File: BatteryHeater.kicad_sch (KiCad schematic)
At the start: 15 parts, among them Q5 Si1442DH, Q7 Si1442DH, Q9 Si1442DH

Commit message: More updates
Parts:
- removed Q5, Q7, Q9: Si1442DH, Package_TO_SOT_SMD:SOT-363_SC-70-6, symbol Transistor_FET:Si1442DH
- removed R23, R27, R31: 10k, Resistor_SMD:R_0603_1608Metric, symbol Device:R_Small
- added D10: GREEN, LED_SMD:LED_0603_1608Metric, symbol Device:LED_Small
- added Q10: IRLML2803, Package_TO_SOT_SMD:SOT-23, symbol Argus-IC:IRLML2803
- added Q19: SIRA99DP-T1-GE3, Package_SO:PowerPAK_SO-8_Single, symbol Transistor_FET:Si7141DP
- added R14, R16: 10k, Resistor_SMD:R_0603_1608Metric, symbol Device:R_Small
- added R15: 1k, Resistor_SMD:R_0603_1608Metric, symbol Device:R_Small
- added R17: 2.7k, Resistor_SMD:R_0603_1608Metric, symbol Device:R_Small
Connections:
- net ENABLE: now also R14.2, R15.2
- net SYSTEM_VSS: now also R22.1, R26.1, R30.1
- net VBUS: now also Q19.1 (S), Q19.2 (S), Q19.3 (S), R16.2; no longer R20.2, R24.2, R28.2
- new net: D10.2 (A), R17.1
- new net: Q10.1 (G), R15.1
- new net: Q10.3 (D), Q19.4 (G), R16.1
- new net GND: D10.1 (K), Q10.2 (S), R14.1
- new net V_HEATER: Q19.5 (D), R17.2, R20.2, R24.2, R28.2
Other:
- moved on the sheet: R20, R21, R22, R24, R25, R26, R28, R29, R30

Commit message: Finalized updates with recommendations and exported files
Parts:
- added F11: 2A, Fuse:Fuse_1206_3216Metric, symbol Device:Fuse_Small
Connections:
- net VBUS: now also F11.1; no longer Q19.1 (S), Q19.2 (S), Q19.3 (S), R16.2
- new net: F11.2, Q19.1 (S), Q19.2 (S), Q19.3 (S), R16.2
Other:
- moved on the sheet: R16

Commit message: uncommitted changes
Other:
- note added: "#TODO Update to larger resistor footprint"
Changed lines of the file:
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@@
+		)
+	)
+	(text "#TODO Update to larger resistor footprint"
+		(exclude_from_sim no)
+		(at 236.22 103.124 0)
+		(effects
+			(font
+				(size 1.27 1.27)
+			)
 		)
 	)
 	(label "V_HEATER"
 		(at 147.32 83.82 0)
+		(fields_autoplaced yes)
 		(effects
 			(font
@@
 		(shape input)
 		(at 80.01 101.6 180)
+		(fields_autoplaced yes)
 		(effects
 			(font

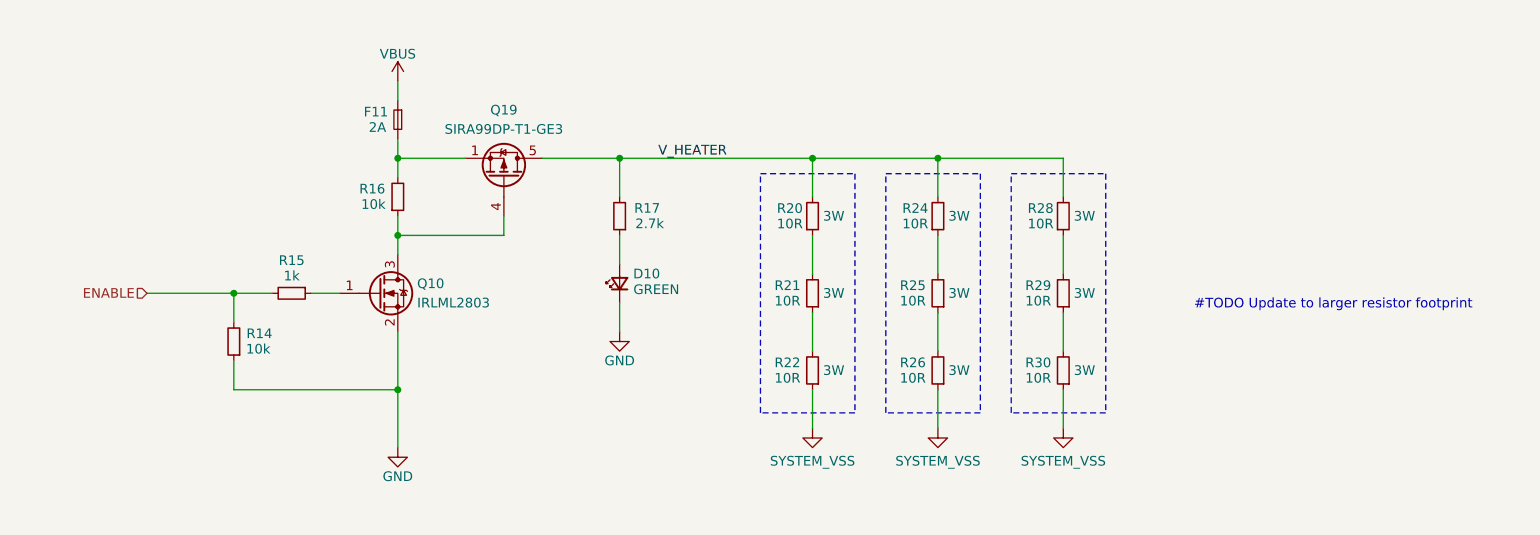
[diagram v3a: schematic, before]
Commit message: Updated FPC connector
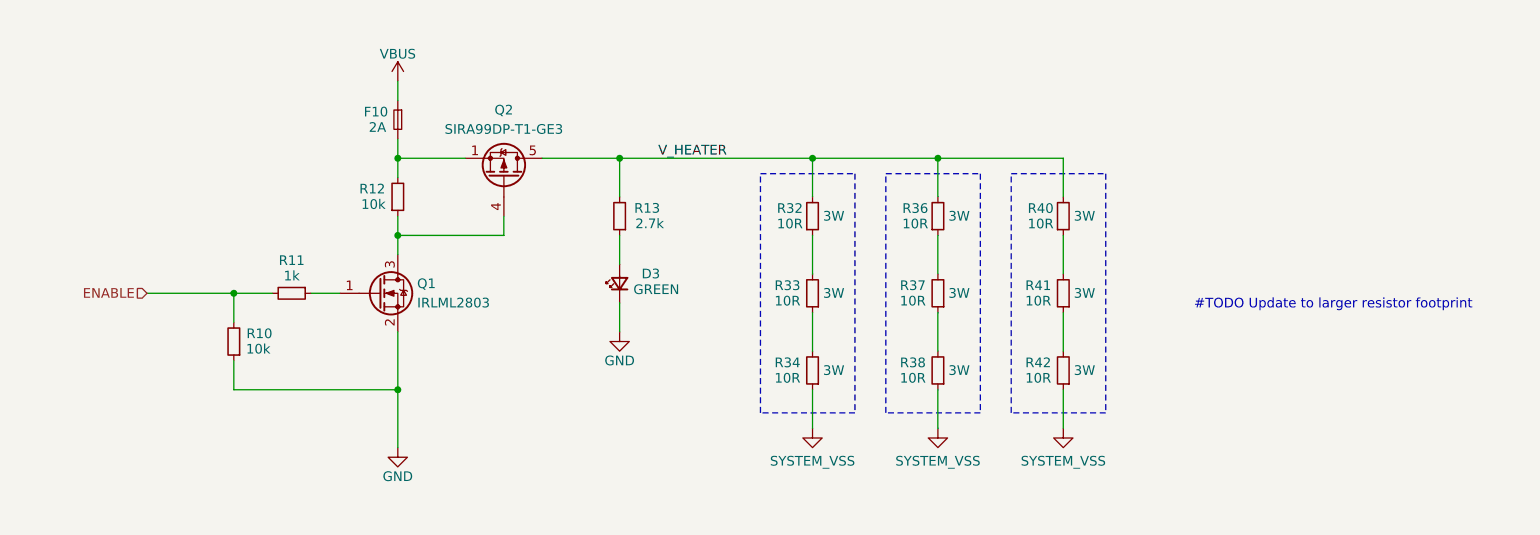
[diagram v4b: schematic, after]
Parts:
- renumbered D10 to D3, F11 to F10, Q10 to Q1, Q19 to Q2, R14 to R10, R15 to R11, R16 to R12, R17 to R13, R20 to R32, R21 to R33, R22 to R34, R24 to R36, R25 to R37, R26 to R38, R28 to R40, R29 to R41, R30 to R42
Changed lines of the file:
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@@
 (kicad_sch
-	(version 20231120)
+	(version 20250114)
 	(generator "eeschema")
-	(generator_version "8.0")
+	(generator_version "9.0")
 	(paper "A4")
 	(title_block
@@
 		(comment 3 "V. Rajesh")
 	)
+	(rectangle
+		(start 177.292 85.852)
+		(end 189.738 117.348)
+		(stroke
+			(width 0)
+			(type dash)
+		)
+		(fill
+			(type none)
+		)
+	)
+	(rectangle
+		(start 193.802 85.852)
+		(end 206.248 117.348)
+		(stroke
+			(width 0)
+			(type dash)
+		)
+		(fill
+			(type none)
+		)
+	)
+	(rectangle
+		(start 160.782 85.852)
+		(end 173.228 117.348)
+		(stroke
+			(width 0)
+			(type dash)
+		)
+		(fill
+			(type none)
+		)
+	)
+	(text "#TODO Update to larger resistor footprint"
+		(exclude_from_sim no)
+		(at 236.22 103.124 0)
+		(effects
+			(font
+				(size 1.27 1.27)
+			)
+		)
+	)
 	(junction
 		(at 113.03 83.82)
@@
 		)
 	)
-	(rectangle
-		(start 177.292 85.852)
-		(end 189.738 117.348)
-		(stroke
-			(width 0)
-			(type dash)
-		)
-		(fill
-			(type none)
-		)
-	)
-	(rectangle
-		(start 193.802 85.852)
-		(end 206.248 117.348)
-		(stroke
-			(width 0)
-			(type dash)
-		)
-		(fill
-			(type none)
-		)
-	)
-	(rectangle
-		(start 160.782 85.852)
-		(end 173.228 117.348)
-		(stroke
-			(width 0)
-			(type dash)
-		)
-		(fill
-			(type none)
-		)
-	)
-	(text "#TODO Update to larger resistor footprint"
-		(exclude_from_sim no)
-		(at 236.22 103.124 0)
+	(label "V_HEATER"
+		(at 147.32 83.82 0)
 		(effects
 			(font
 				(size 1.27 1.27)
 			)
-		)
-	)
-	(label "V_HEATER"
-		(at 147.32 83.82 0)
-		(fields_autoplaced yes)
-		(effects
-			(font
-				(size 1.27 1.27)
-			)
 			(justify left bottom)
 		)
@@
 		(shape input)
 		(at 80.01 101.6 180)
-		(fields_autoplaced yes)
 		(effects
 			(font
@@
 		(on_board yes)
 		(dnp no)
-		(property "Reference" "R28"
+		(property "Reference" "R40"
 			(at 199.39 90.424 0)
 			(effects
@@
 		(on_board yes)
 		(dnp no)
-		(property "Reference" "R17"
+		(property "Reference" "R13"
 			(at 147.574 89.662 0)
 			(effects
@@
 		(on_board yes)
 		(dnp no)
-		(property "Reference" "#PWR014"
+		(property "Reference" "#PWR057"
 			(at 167.64 125.73 0)
 			(effects
@@
 		(on_board yes)
 		(dnp no)
-		(property "Reference" "Q10"
+		(property "Reference" "Q1"
 			(at 115.57 100.33 0)
 			(effects
@@
 		(on_board yes)
 		(dnp no)
-		(property "Reference" "R14"
+		(property "Reference" "R10"
 			(at 96.52 106.172 0)
 			(effects
@@
 		(on_board yes)
 		(dnp no)
-		(property "Reference" "R25"
+		(property "Reference" "R37"
 			(at 180.848 100.584 0)
 			(effects
@@
 		(on_board yes)
 		(dnp no)
-		(property "Reference" "R15"
+		(property "Reference" "R11"
 			(at 99.06 97.282 90)
 			(effects
@@
 		(on_board yes)
 		(dnp no)
-		(property "Reference" "R29"
+		(property "Reference" "R41"
 			(at 197.358 100.584 0)
 			(effects
@@
 		(on_board yes)
 		(dnp no)
-		(property "Reference" "R22"
+		(property "Reference" "R34"
 			(at 164.338 110.744 0)
 			(effects
@@
 		(on_board yes)
 		(dnp no)
-		(property "Reference" "R26"
+		(property "Reference" "R38"
 			(at 180.848 110.744 0)
 			(effects
@@
 		(on_board yes)
 		(dnp no)
-		(property "Reference" "#PWR024"
+		(property "Reference" "#PWR023"
 			(at 200.66 125.73 0)
 			(effects
@@
 		(on_board yes)
 		(dnp no)
-		(property "Reference" "F11"
+		(property "Reference" "F10"
 			(at 111.76 77.724 90)
 			(effects
@@
 		(on_board yes)
 		(dnp no)
-		(property "Reference" "#PWR015"
+		(property "Reference" "#PWR09"
 			(at 113.03 77.47 0)
 			(effects
@@
 		(on_board yes)
 		(dnp no)
-		(property "Reference" "R24"
+		(property "Reference" "R36"
 			(at 182.88 90.424 0)
 			(effects
@@
 		(on_board yes)
 		(dnp no)
-		(property "Reference" "R20"
+		(property "Reference" "R32"
 			(at 166.37 90.424 0)
 			(effects
@@
 		(on_board yes)
 		(dnp no)
-		(property "Reference" "Q19"
+		(property "Reference" "Q2"
 			(at 127 77.47 90)
 			(effects
@@
 		(on_board yes)
 		(dnp no)
-		(property "Reference" "R30"
+		(property "Reference" "R42"
 			(at 197.358 110.744 0)
 			(effects
@@
 		(on_board yes)
 		(dnp no)
-		(property "Reference" "#GND04"
+		(property "Reference" "#GND01"
 			(at 113.03 121.92 0)
 			(effects
@@
 		(on_board yes)
 		(dnp no)
-		(property "Reference" "D10"
+		(property "Reference" "D3"
 			(at 147.574 98.298 90)
 			(effects
@@
 		(on_board yes)
 		(dnp no)
-		(property "Reference" "R16"
+		(property "Reference" "R12"
 			(at 107.95 87.122 0)
 			(effects
@@
 		(on_board yes)
 		(dnp no)
-		(property "Reference" "#GND05"
+		(property "Reference" "#GND03"
 			(at 142.24 106.68 0)
 			(effects
@@
 		(on_board yes)
 		(dnp no)
-		(property "Reference" "#PWR018"
+		(property "Reference" "#PWR017"
 			(at 184.15 125.73 0)
 			(effects
@@
 		(on_board yes)
 		(dnp no)
-		(property "Reference" "R21"
+		(property "Reference" "R33"
 			(at 164.338 100.584 0)
 			(effects

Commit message: v3.1 Updates
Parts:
- R27: renamed from R13; value 2.7k -> 10k
- renumbered D3 to D5, Q2 to Q5, Q1 to Q6, R10 to R24, R11 to R25, R12 to R26, R32 to R28, R33 to R29, R34 to R30, R36 to R31, R37 to R32, R38 to R33, R40 to R34, R41 to R35, R42 to R36
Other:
- note removed: "#TODO Update to larger resistor footprint"

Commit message: Idk some changes
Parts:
- D5: DIS Digi-Key -> (none); DPN 511-1584-1-ND -> (none); MFR Rohm -> (none); MPN SML-E12M8WT86 -> C2909774
- Q5: MPN (none) -> C3289459
- Q6: MPN (none) -> C2590
- R24, R26: DIS Digi-Key -> (none); DPN 311-10.0KHRCT-ND -> (none); MFR Yageo -> (none); MPN RC0603FR-0710KL -> C2479067
- R25: DIS Digi-Key -> (none); DPN A129693CT-ND -> (none); MFR TE -> (none); MPN CRGCQ0603F2K7 -> C2484712
- R27: DIS Digi-Key -> (none); DPN A129693CT-ND -> (none); MFR TE -> (none); MPN CRGCQ0603F2K7 -> C2479067
- R28, R29, R30, R31, R32, R33, R34, R35, R36: footprint Resistor_SMD:R_2010_5025Metric -> Resistor_SMD:R_2512_6332Metric
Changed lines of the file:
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@@
 			)
 		)
-		(property "Footprint" "Resistor_SMD:R_2010_5025Metric"
+		(property "Footprint" "Resistor_SMD:R_2512_6332Metric"
 			(at 200.66 91.44 0)
 			(effects
@@
 			)
 		)
-		(property "DIS" "Digi-Key"
+		(property "MPN" "C2479067"
 			(at 142.24 91.44 0)
 			(effects
@@
 					(size 1.27 1.27)
 				)
-				(justify left bottom)
-				(hide yes)
-			)
-		)
-		(property "DPN" "A129693CT-ND"
-			(at 142.24 91.44 0)
-			(effects
-				(font
-					(size 1.27 1.27)
-				)
-				(justify left bottom)
-				(hide yes)
-			)
-		)
-		(property "MFR" "TE"
-			(at 142.24 91.44 0)
-			(effects
-				(font
-					(size 1.27 1.27)
-				)
-				(justify left bottom)
-				(hide yes)
-			)
-		)
-		(property "MPN" "CRGCQ0603F2K7"
-			(at 142.24 91.44 0)
-			(effects
-				(font
-					(size 1.27 1.27)
-				)
-				(justify left bottom)
 				(hide yes)
 			)
@@
 			)
 		)
+		(property "MPN" "C2590"
+			(at 113.03 101.6 0)
+			(effects
+				(font
+					(size 1.27 1.27)
+				)
+				(hide yes)
+			)
+		)
 		(pin "1"
 		)
@@
 			)
 		)
-		(property "DIS" "Digi-Key"
+		(property "MPN" "C2479067"
 			(at 91.44 107.95 0)
 			(effects
@@
 					(size 1.27 1.27)
 				)
-				(justify left bottom)
-				(hide yes)
-			)
-		)
-		(property "DPN" "311-10.0KHRCT-ND"
-			(at 91.44 107.95 0)
-			(effects
-				(font
-					(size 1.27 1.27)
-				)
-				(justify left bottom)
-				(hide yes)
-			)
-		)
-		(property "MFR" "Yageo"
-			(at 91.44 107.95 0)
-			(effects
-				(font
-					(size 1.27 1.27)
-				)
-				(justify left bottom)
-				(hide yes)
-			)
-		)
-		(property "MPN" "RC0603FR-0710KL"
-			(at 91.44 107.95 0)
-			(effects
-				(font
-					(size 1.27 1.27)
-				)
-				(justify left bottom)
 				(hide yes)
 			)
@@
 			)
 		)
-		(property "Footprint" "Resistor_SMD:R_2010_5025Metric"
+		(property "Footprint" "Resistor_SMD:R_2512_6332Metric"
 			(at 184.15 101.6 0)
 			(effects
@@
 			)
 		)
-		(property "DIS" "Digi-Key"
-			(at 99.06 101.6 0)
-			(effects
-				(font
-					(size 1.27 1.27)
-				)
-				(justify left bottom)
-				(hide yes)
-			)
-		)
-		(property "DPN" "A129693CT-ND"
-			(at 99.06 101.6 0)
-			(effects
-				(font
-					(size 1.27 1.27)
-				)
-				(justify left bottom)
-				(hide yes)
-			)
-		)
-		(property "MFR" "TE"
-			(at 99.06 101.6 0)
-			(effects
-				(font
-					(size 1.27 1.27)
-				)
-				(justify left bottom)
-				(hide yes)
-			)
-		)
-		(property "MPN" "CRGCQ0603F2K7"
-			(at 99.06 101.6 0)
-			(effects
-				(font
-					(size 1.27 1.27)
-				)
-				(justify left bottom)
+		(property "MPN" "C2484712"
+			(at 99.06 101.6 90)
+			(effects
+				(font
+					(size 1.27 1.27)
+				)
 				(hide yes)
 			)
@@
 			)
 		)
-		(property "Footprint" "Resistor_SMD:R_2010_5025Metric"
+		(property "Footprint" "Resistor_SMD:R_2512_6332Metric"
 			(at 200.66 101.6 0)
 			(effects
@@
 			)
 		)
-		(property "Footprint" "Resistor_SMD:R_2010_5025Metric"
+		(property "Footprint" "Resistor_SMD:R_2512_6332Metric"
 			(at 167.64 111.76 0)
 			(effects
@@
 			)
 		)
-		(property "Footprint" "Resistor_SMD:R_2010_5025Metric"
+		(property "Footprint" "Resistor_SMD:R_2512_6332Metric"
 			(at 184.15 111.76 0)
 			(effects
@@
 			)
 		)
-		(property "Footprint" "Resistor_SMD:R_2010_5025Metric"
+		(property "Footprint" "Resistor_SMD:R_2512_6332Metric"
 			(at 184.15 91.44 0)
 			(effects
@@
 			)
 		)
-		(property "Footprint" "Resistor_SMD:R_2010_5025Metric"
+		(property "Footprint" "Resistor_SMD:R_2512_6332Metric"
 			(at 167.64 91.44 0)
 			(effects
@@
 			)
 		)
+		(property "MPN" "C3289459"
+			(at 127 86.36 90)
+			(effects
+				(font
+					(size 1.27 1.27)
+				)
+				(hide yes)
+			)
+		)
 		(pin "5"
 		)
@@
 			)
 		)
-		(property "Footprint" "Resistor_SMD:R_2010_5025Metric"
+		(property "Footprint" "Resistor_SMD:R_2512_6332Metric"
 			(at 200.66 111.76 0)
 			(effects
@@
 			)
 		)
-		(property "DIS" "Digi-Key"
+		(property "MPN" "C2909774"
 			(at 142.24 100.33 0)
 			(effects
@@
 				)
 				(justify left bottom)
-				(hide yes)
-			)
-		)
-		(property "DPN" "511-1584-1-ND"
-			(at 142.24 100.33 0)
-			(effects
-				(font
-					(size 1.27 1.27)
-				)
-				(justify left bottom)
-				(hide yes)
-			)
-		)
-		(property "MFR" "Rohm"
-			(at 142.24 100.33 0)
-			(effects
-				(font
-					(size 1.27 1.27)
-				)
-				(justify left bottom)
-				(hide yes)
-			)
-		)
-		(property "MPN" "SML-E12M8WT86"
-			(at 142.24 100.33 0)
-			(effects
-				(font
-					(size 1.27 1.27)
-				)
-				(justify left bottom)
-				(hide yes)
-			)
-		)
-		(property "Sim.Pin" "1=K 2=A"
-			(at 142.24 100.33 0)
-			(effects
-				(font
-					(size 1.27 1.27)
-				)
 				(hide yes)
 			)
@@
 			)
 		)
-		(property "DIS" "Digi-Key"
+		(property "MPN" "C2479067"
 			(at 113.03 88.9 0)
 			(effects
@@
 					(size 1.27 1.27)
 				)
-				(justify left bottom)
-				(hide yes)
-			)
-		)
-		(property "DPN" "311-10.0KHRCT-ND"
-			(at 113.03 88.9 0)
-			(effects
-				(font
-					(size 1.27 1.27)
-				)
-				(justify left bottom)
-				(hide yes)
-			)
-		)
-		(property "MFR" "Yageo"
-			(at 113.03 88.9 0)
-			(effects
-				(font
-					(size 1.27 1.27)
-				)
-				(justify left bottom)
-				(hide yes)
-			)
-		)
-		(property "MPN" "RC0603FR-0710KL"
-			(at 113.03 88.9 0)
-			(effects
-				(font
-					(size 1.27 1.27)
-				)
-				(justify left bottom)
 				(hide yes)
 			)
@@
 			)
 		)
-		(property "Footprint" "Resistor_SMD:R_2010_5025Metric"
+		(property "Footprint" "Resistor_SMD:R_2512_6332Metric"
 			(at 167.64 101.6 0)
 			(effects

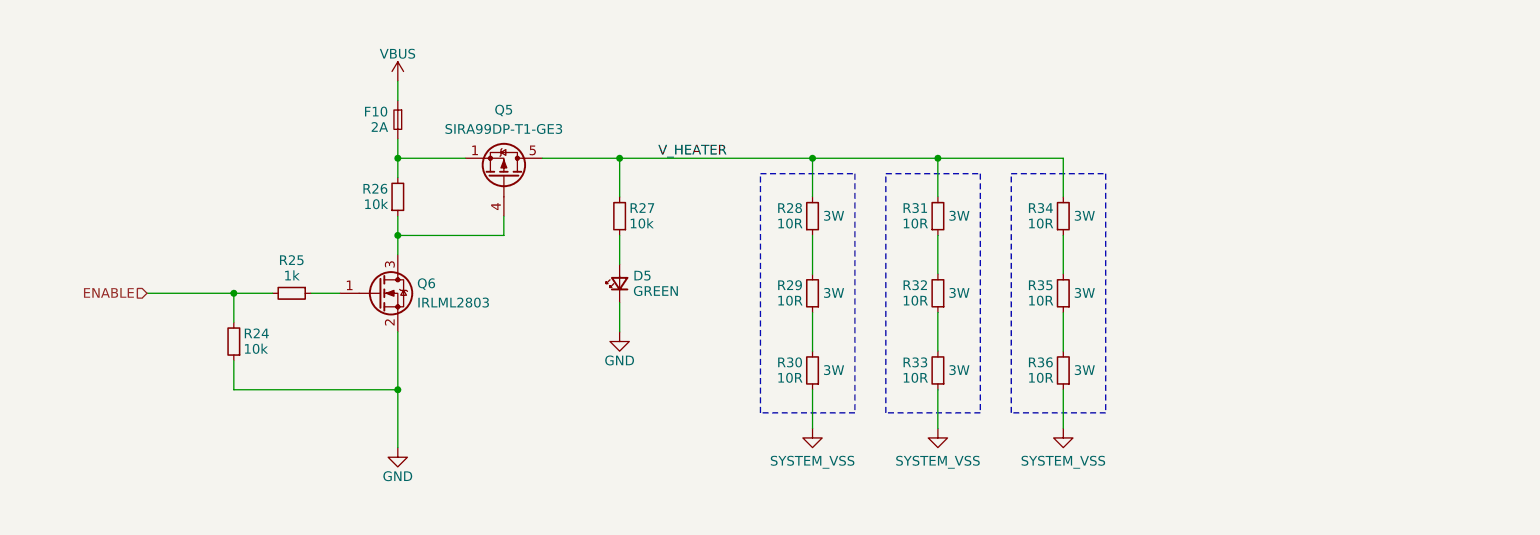
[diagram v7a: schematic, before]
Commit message: v3.2 Updates
Added 0ohm bypass. Opto-isolated heater enables
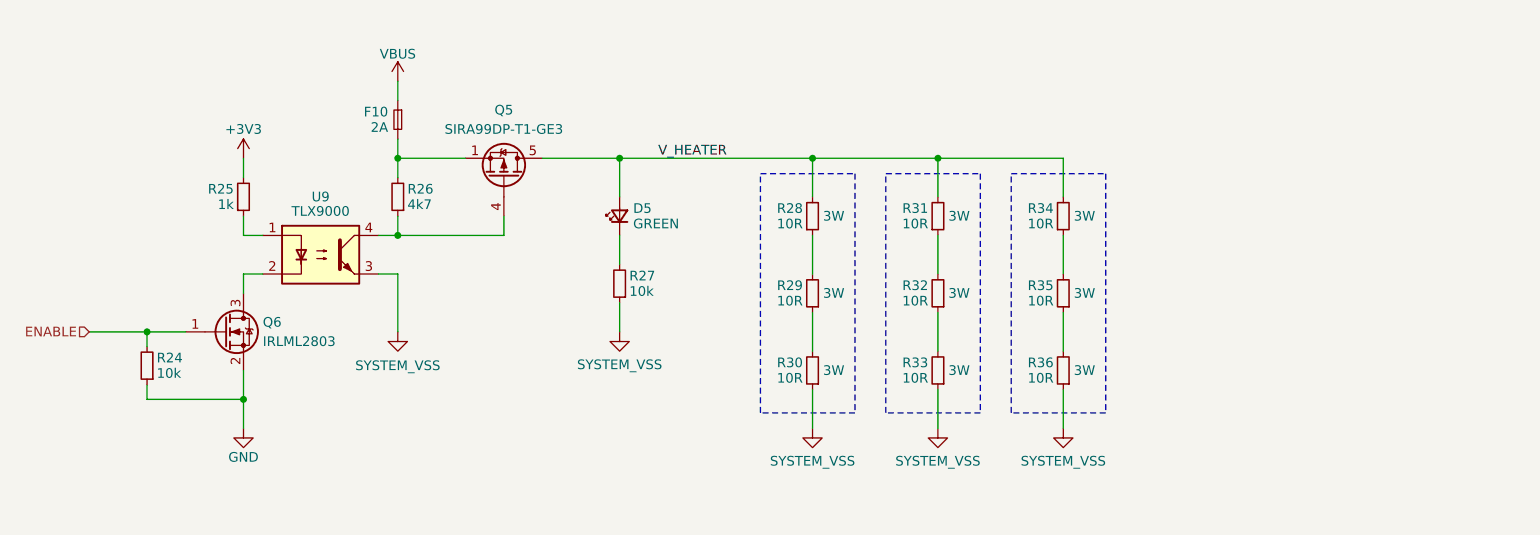
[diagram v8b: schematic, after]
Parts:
- added U9: TLX9000, Package_SO:SOIC-4_4.55x2.6mm_P1.27mm, symbol Isolator:Optocoupler_DC_PhotoNPN_AKEC
- R25: MPN C2484712 -> C2479067
- R26: value 10k -> 4k7
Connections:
- net ENABLE: now also Q6.1 (G); no longer R25.2
- net GND: no longer D5.1 (K)
- net SYSTEM_VSS: now also R27.1, U9.3
- net V_HEATER: now also D5.2 (A); no longer R27.2
- net at R25.1: now also U9.1; no longer Q6.1 (G)
- net at Q5.4 (G), R26.1: now also U9.4; no longer Q6.3 (D)
- new net: D5.1 (K), R27.2
- new net: Q6.3 (D), U9.2
- new net +3V3: R25.2
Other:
- moved on the sheet: D5, R26, R27
